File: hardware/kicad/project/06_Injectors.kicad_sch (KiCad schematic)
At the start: 0 parts

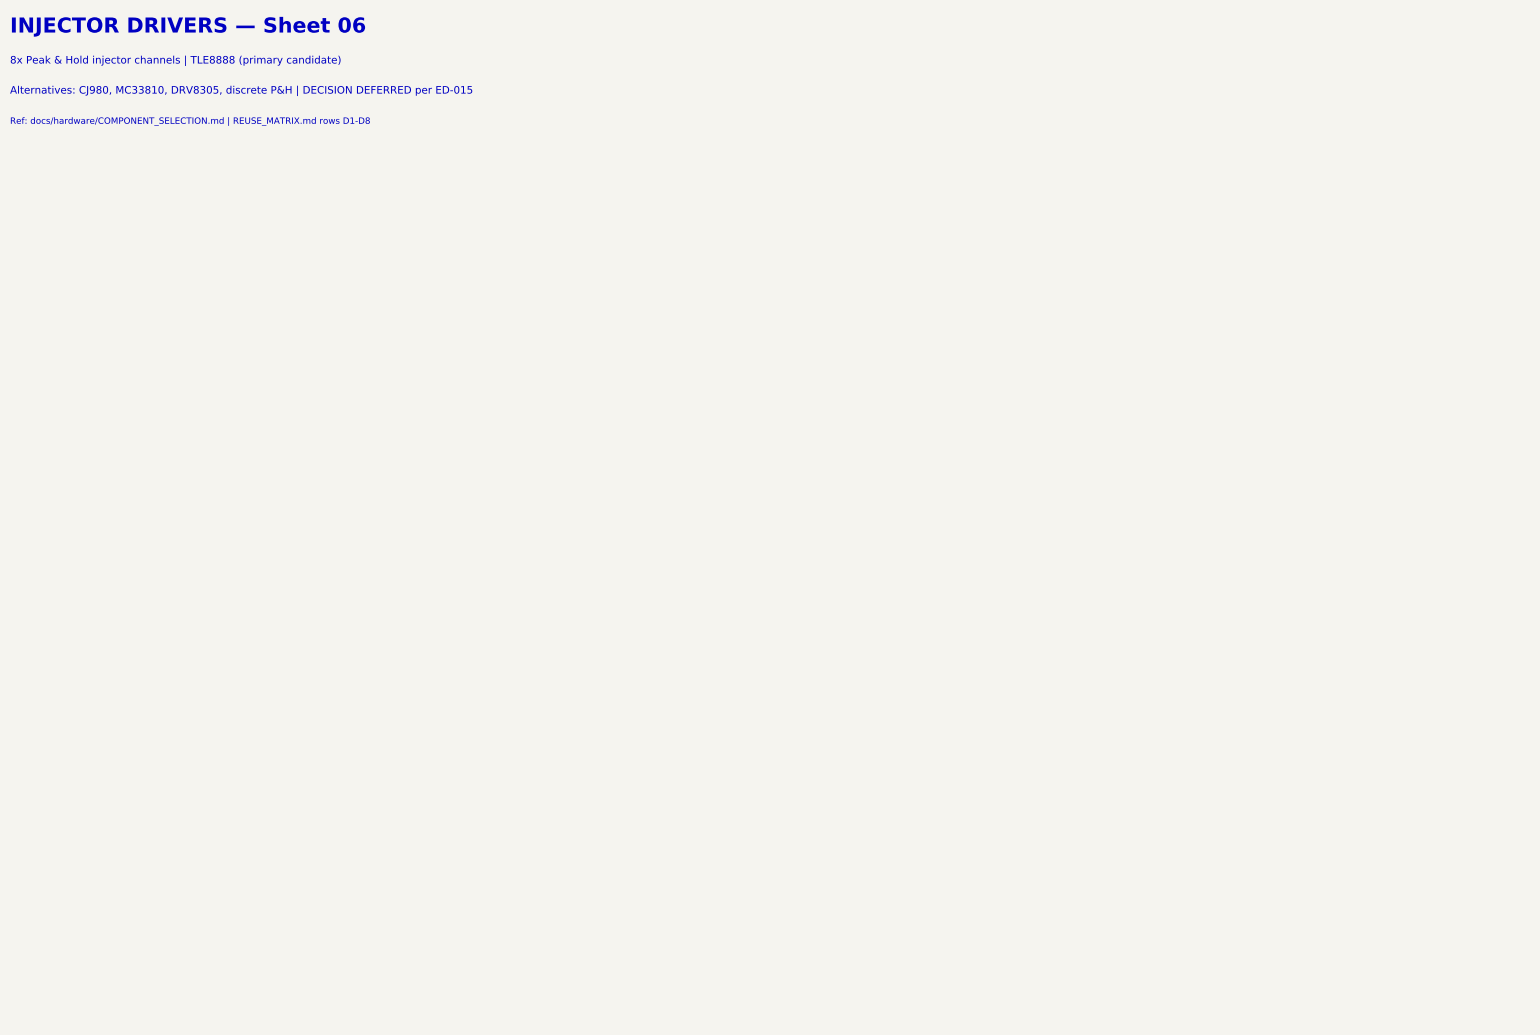
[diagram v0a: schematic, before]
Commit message: feat(hardware): TB-HW-002 — populate all 12 schematic sheets with components
Populated 235 component symbols across all 12 KiCad schematic sheets:
- 01_Power: Reverse polarity, TVS (SMCJ33A), buck (LMR33630), LDO (TPS7A1633), VREF (REF5050) — 30 symbols
- 02_MCU: S32K344 (6 units), clock (40MHz+32kHz), decoupling, reset, boot config, LEDs — 30 symbols
- 03_CAN: 4x TJA1043 with CM chokes (ACT45B-510), split termination, bus filter caps — 36 symbols
- 04_USB: Molex USB-C, TPD2EUSB30 ESD, CC resistors, eFuse, Ethernet PHY footprint — 9 symbols
- 05_Inputs: 8 analog channels (RC+clamp), 2x CJ125 WBO2, 2x TLE2072 knock amps — 50 symbols
- 06_Injectors: TLE8888-2QK (8-ch P&H), flyback diodes, current sense — 14 symbols
- 07_Ignition: 6x ISL9V3040S3 IGBTs with gate resistors (100R), pull-downs (10k) — 24 symbols
- 08_Outputs: DRV8873 ETC H-bridge, TLE8110ED low-side (boost+relays), BTS4140N tach — 12 symbols
- 09_Protection: TPS3850G33 watchdog, safe-state FET, ESD diodes (PESD5V0) — 14 symbols
- 10_Connectors: 42-pin Deutsch DTM (2 units), 2x CAN 4-pin, diagnostic 4-pin — 5 symbols
- 11_Programming: TC2050 SWD, 8 test points, production security notes — 11 symbols
- 00_Cover: Block diagram, BOM summary, spec references, revision history

Symbol library: 18 custom symbols with complete pin assignments
Components from COMPONENT_SELECTION.md r0.1
42-pin connector per INTERFACE_SPECIFICATION.md (authority)
All MCU pins per MCU_SELECTION.md pin allocation
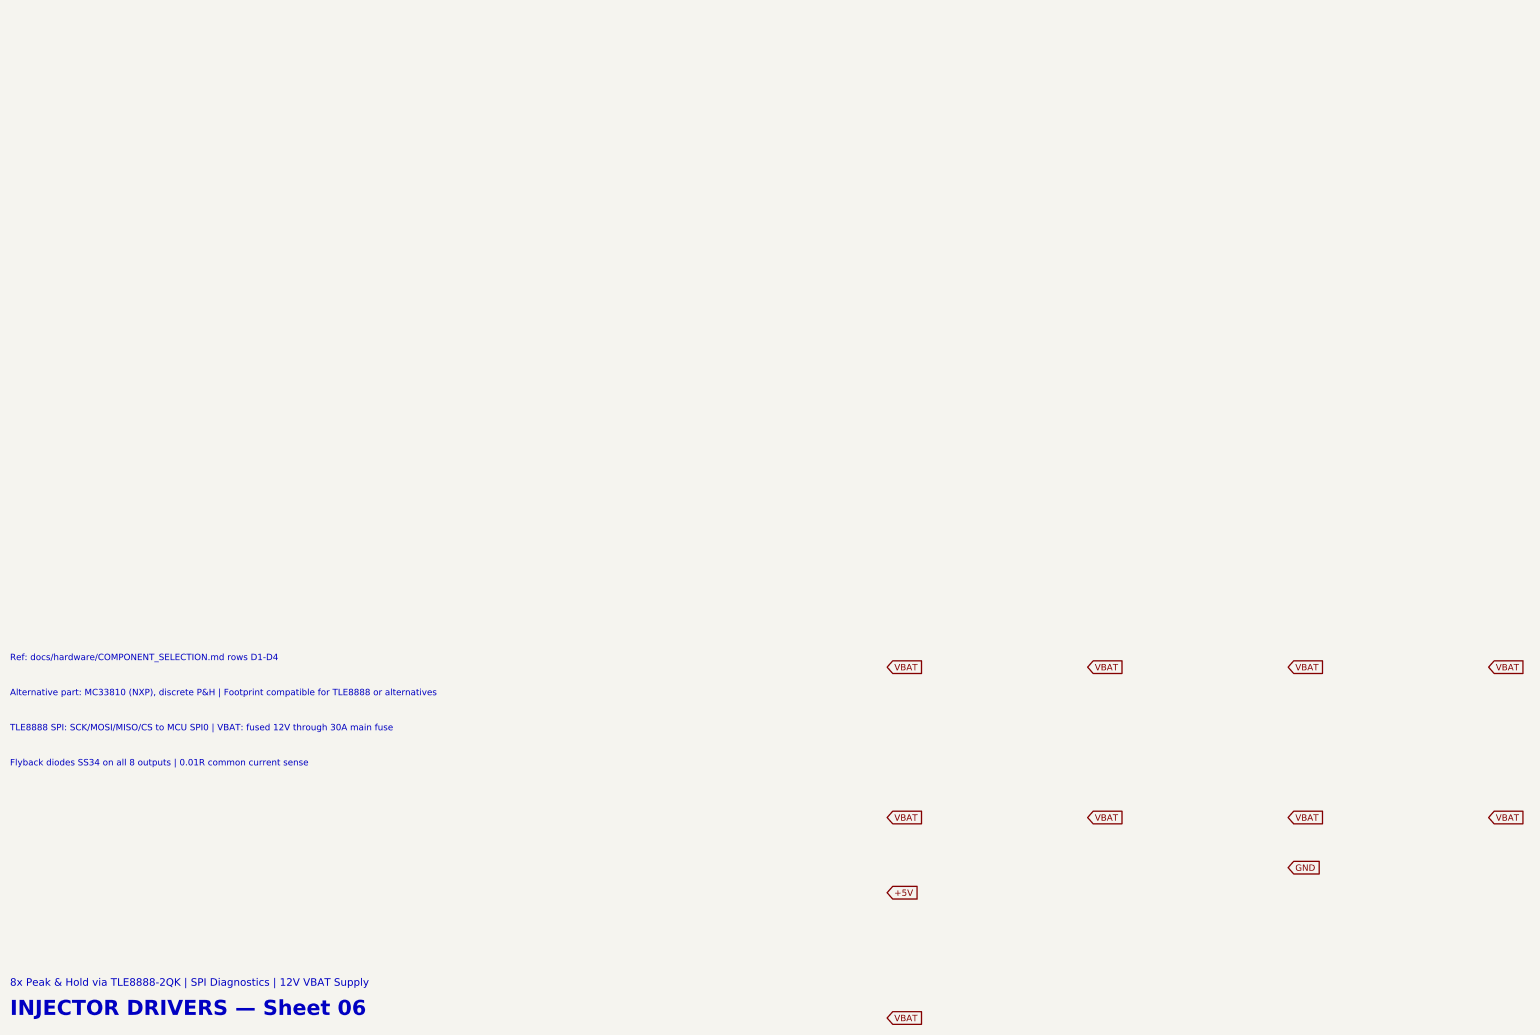
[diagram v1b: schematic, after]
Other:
- note added: "8x Peak & Hold via TLE8888-2QK | SPI Diagnostics | 12V VBAT Supply"
- note added: "Alternative part: MC33810 (NXP), discrete P&H | Footprint compatible for TLE8888 or alternatives"
- note added: "Flyback diodes SS34 on all 8 outputs | 0.01R common current sense"
- note added: "Ref: docs/hardware/COMPONENT_SELECTION.md rows D1-D4"
- note added: "TLE8888 SPI: SCK/MOSI/MISO/CS to MCU SPI0 | VBAT: fused 12V through 30A main fuse"
- note removed: "8x Peak & Hold injector channels | TLE8888 (primary candidate)"
- note removed: "Alternatives: CJ980, MC33810, DRV8305, discrete P&H | DECISION DEFERRED per ED-015"
- note removed: "Ref: docs/hardware/COMPONENT_SELECTION.md | REUSE_MATRIX.md rows D1-D8"
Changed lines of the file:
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@@
-(kicad_sch (version 20240108) (generator "eeschema")
+(kicad_sch (version 20240108) (generator "7100CPT-schematic-gen")
   (paper "A3")
   (title_block
     (title "7100CPT ECU — Peak & Hold Injector Drivers x8")
     (date "2026-07-03")
-    (rev "0.1")
+    (rev "0.2")
     (company "${COMPANY}")
-    (comment 1 "Peak & Hold x8 (TLE8888 or alternative), current sense, SPI diagnostics")
+    (comment 1 "TLE8888-2QK, 8-ch peak & hold, SPI diagnostics")
     (comment 2 "NXP S32K344 | rusEFI Firmware | IPC Class 3")
     (comment 3 "High-Tg FR-4 (TG170+) | ENIG | 1.6 mm")
-    (comment 4 "REUSE_MATRIX.md — NXP Reference Following")
+    (comment 4 "Phase 0 Approved | REUSE_MATRIX gate passed")
     (comment 5 "-40C to +85C | IP67 Target | 6-Layer")
   )
-  (symbol_instances)
-  (text "INJECTOR DRIVERS — Sheet 06"
-    (at 25 24 0) (effects (font (size 3.0 3.0) bold) (justify left bottom)))
-  (text "8x Peak & Hold injector channels | TLE8888 (primary candidate)"
-    (at 25 30 0) (effects (font (size 1.5 1.5)) (justify left bottom)))
-  (text "Alternatives: CJ980, MC33810, DRV8305, discrete P&H | DECISION DEFERRED per ED-015"
-    (at 25 36 0) (effects (font (size 1.5 1.5)) (justify left bottom)))
-  (text "Ref: docs/hardware/COMPONENT_SELECTION.md | REUSE_MATRIX.md rows D1-D8"
-    (at 25 42 0) (effects (font (size 1.27 1.27)) (justify left bottom)))
+  (symbol_instances
+  (symbol (lib_id "7100CPT:TLE8888_2QK") (at 200 200 0) (unit 1)
+    (exclude_from_sim yes) (in_bom yes) (on_board yes) (dnp no)
+    (property "Reference" "U40" (at 200 200 0) (effects (font (size 1.27 1.27))))
+    (property "Value" "TLE8888-2QK" (at 200 193.65 0) (effects (font (size 1.27 1.27))))
+  )
+  (symbol (lib_id "Device:D_Schottky") (at 200 170 0) (unit 1)
+    (exclude_from_sim yes) (in_bom yes) (on_board yes) (dnp no)
+    (property "Reference" "D30" (at 200 170 0) (effects (font (size 1.27 1.27))))
+    (property "Value" "SS34" (at 200 163.65 0) (effects (font (size 1.27 1.27))))
+  )
+  (symbol (lib_id "Device:D_Schottky") (at 240 170 0) (unit 1)
+    (exclude_from_sim yes) (in_bom yes) (on_board yes) (dnp no)
+    (property "Reference" "D31" (at 240 170 0) (effects (font (size 1.27 1.27))))
+    (property "Value" "SS34" (at 240 163.65 0) (effects (font (size 1.27 1.27))))
+  )
+  (symbol (lib_id "Device:D_Schottky") (at 280 170 0) (unit 1)
+    (exclude_from_sim yes) (in_bom yes) (on_board yes) (dnp no)
+    (property "Reference" "D32" (at 280 170 0) (effects (font (size 1.27 1.27))))
+    (property "Value" "SS34" (at 280 163.65 0) (effects (font (size 1.27 1.27))))
+  )
+  (symbol (lib_id "Device:D_Schottky") (at 320 170 0) (unit 1)
+    (exclude_from_sim yes) (in_bom yes) (on_board yes) (dnp no)
+    (property "Reference" "D33" (at 320 170 0) (effects (font (size 1.27 1.27))))
+    (property "Value" "SS34" (at 320 163.65 0) (effects (font (size 1.27 1.27))))
+  )
+  (symbol (lib_id "Device:D_Schottky") (at 200 140 0) (unit 1)
+    (exclude_from_sim yes) (in_bom yes) (on_board yes) (dnp no)
+    (property "Reference" "D34" (at 200 140 0) (effects (font (size 1.27 1.27))))
+    (property "Value" "SS34" (at 200 133.65 0) (effects (font (size 1.27 1.27))))
+  )
+  (symbol (lib_id "Device:D_Schottky") (at 240 140 0) (unit 1)
+    (exclude_from_sim yes) (in_bom yes) (on_board yes) (dnp no)
+    (property "Reference" "D35" (at 240 140 0) (effects (font (size 1.27 1.27))))
+    (property "Value" "SS34" (at 240 133.65 0) (effects (font (size 1.27 1.27))))
+  )
+  (symbol (lib_id "Device:D_Schottky") (at 280 140 0) (unit 1)
+    (exclude_from_sim yes) (in_bom yes) (on_board yes) (dnp no)
+    (property "Reference" "D36" (at 280 140 0) (effects (font (size 1.27 1.27))))
+    (property "Value" "SS34" (at 280 133.65 0) (effects (font (size 1.27 1.27))))
+  )
+  (symbol (lib_id "Device:D_Schottky") (at 320 140 0) (unit 1)
+    (exclude_from_sim yes) (in_bom yes) (on_board yes) (dnp no)
+    (property "Reference" "D37" (at 320 140 0) (effects (font (size 1.27 1.27))))
+    (property "Value" "SS34" (at 320 133.65 0) (effects (font (size 1.27 1.27))))
+  )
+  (symbol (lib_id "Device:CP") (at 200 220 0) (unit 1)
+    (exclude_from_sim yes) (in_bom yes) (on_board yes) (dnp no)
+    (property "Reference" "C100" (at 200 220 0) (effects (font (size 1.27 1.27))))
+    (property "Value" "470uF_35V_Elec" (at 200 213.65 0) (effects (font (size 1.27 1.27))))
+  )
+  (symbol (lib_id "Device:C") (at 230 220 0) (unit 1)
+    (exclude_from_sim yes) (in_bom yes) (on_board yes) (dnp no)
+    (property "Reference" "C101" (at 230 220 0) (effects (font (size 1.27 1.27))))
+    (property "Value" "100nF_50V_X7R" (at 230 213.65 0) (effects (font (size 1.27 1.27))))
+  )
+  (symbol (lib_id "Device:R") (at 280 200 0) (unit 1)
+    (exclude_from_sim yes) (in_bom yes) (on_board yes) (dnp no)
+    (property "Reference" "R70" (at 280 200 0) (effects (font (size 1.27 1.27))))
+    (property "Value" "0.01R_2W_2512" (at 280 193.65 0) (effects (font (size 1.27 1.27))))
+  )
+  (symbol (lib_id "Device:C") (at 180 210 0) (unit 1)
+    (exclude_from_sim yes) (in_bom yes) (on_board yes) (dnp no)
+    (property "Reference" "C102" (at 180 210 0) (effects (font (size 1.27 1.27))))
+    (property "Value" "100nF_50V_X7R" (at 180 203.65 0) (effects (font (size 1.27 1.27))))
+  )
+  (symbol (lib_id "Device:C") (at 220 210 0) (unit 1)
+    (exclude_from_sim yes) (in_bom yes) (on_board yes) (dnp no)
+    (property "Reference" "C103" (at 220 210 0) (effects (font (size 1.27 1.27))))
+    (property "Value" "10uF_25V_X7R" (at 220 203.65 0) (effects (font (size 1.27 1.27))))
+  )
+  )
+  (text "INJECTOR DRIVERS — Sheet 06" (at 25 220 0) (effects (font (size 3.0 3.0) bold) (justify left bottom)))
+  (text "8x Peak & Hold via TLE8888-2QK | SPI Diagnostics | 12V VBAT Supply" (at 25 214 0) (effects (font (size 1.5 1.5)) (justify left bottom)))
+  (text "Flyback diodes SS34 on all 8 outputs | 0.01R common current sense" (at 25 170 0) (effects (font (size 1.27 1.27)) (justify left bottom)))
+  (text "TLE8888 SPI: SCK/MOSI/MISO/CS to MCU SPI0 | VBAT: fused 12V through 30A main fuse" (at 25 163 0) (effects (font (size 1.27 1.27)) (justify left bottom)))
+  (text "Alternative part: MC33810 (NXP), discrete P&H | Footprint compatible for TLE8888 or alternatives" (at 25 156 0) (effects (font (size 1.27 1.27)) (justify left bottom)))
+  (text "Ref: docs/hardware/COMPONENT_SELECTION.md rows D1-D4" (at 25 149 0) (effects (font (size 1.27 1.27)) (justify left bottom)))
+  (global_label "VBAT" (shape input) (at 200 180 0) (effects (font (size 1.27 1.27))))
+  (global_label "VBAT" (shape input) (at 240 180 0) (effects (font (size 1.27 1.27))))
+  (global_label "VBAT" (shape input) (at 280 180 0) (effects (font (size 1.27 1.27))))
+  (global_label "VBAT" (shape input) (at 320 180 0) (effects (font (size 1.27 1.27))))
+  (global_label "VBAT" (shape input) (at 200 150 0) (effects (font (size 1.27 1.27))))
+  (global_label "VBAT" (shape input) (at 240 150 0) (effects (font (size 1.27 1.27))))
+  (global_label "VBAT" (shape input) (at 280 150 0) (effects (font (size 1.27 1.27))))
+  (global_label "VBAT" (shape input) (at 320 150 0) (effects (font (size 1.27 1.27))))
+  (global_label "VBAT" (shape input) (at 200 220 0) (effects (font (size 1.27 1.27))))
+  (global_label "+5V" (shape input) (at 200 195 0) (effects (font (size 1.27 1.27))))
+  (global_label "GND" (shape input) (at 280 190 0) (effects (font (size 1.27 1.27))))
   (sheet_instances
     (path "/06_injectors/" (page "7"))
